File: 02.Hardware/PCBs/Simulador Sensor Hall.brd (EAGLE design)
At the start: 78.5 x 44.8 mm, 23 parts

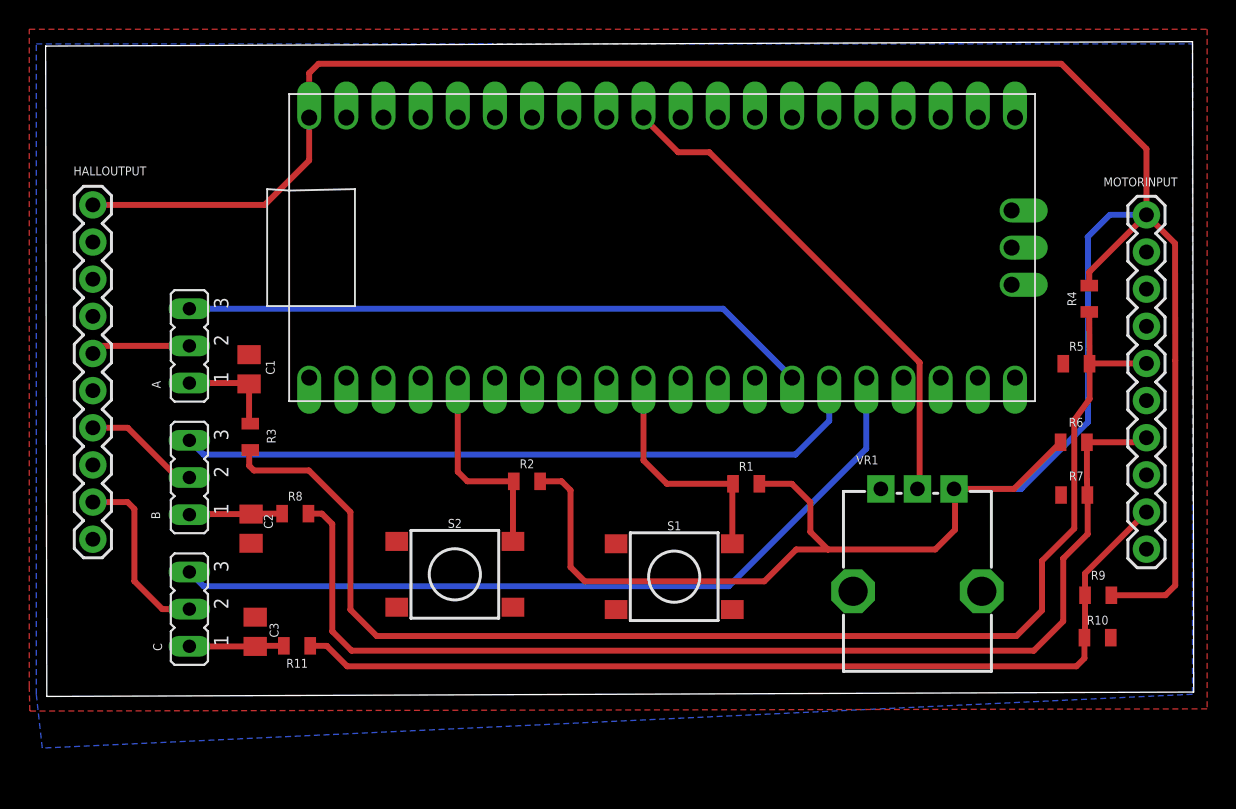
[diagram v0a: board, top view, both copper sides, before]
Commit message: Resistencias en serie en los pulsadores y potenciometro
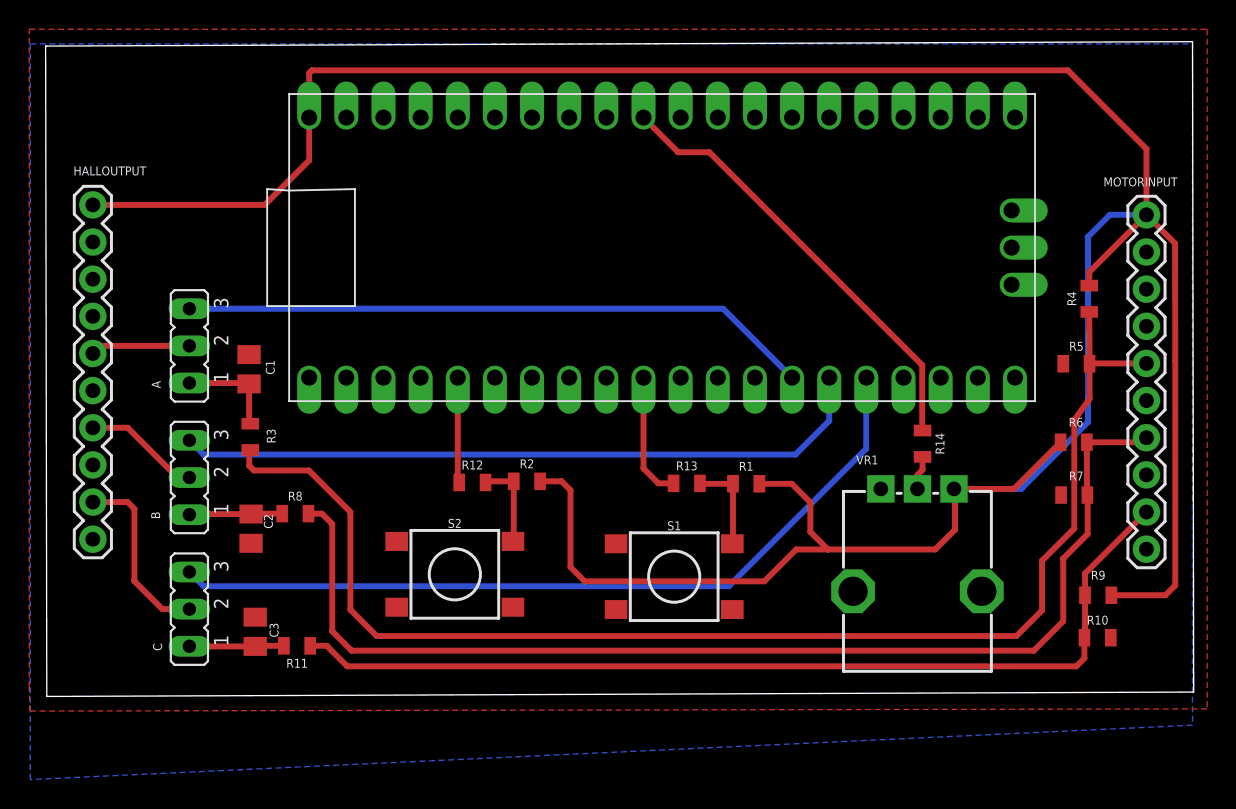
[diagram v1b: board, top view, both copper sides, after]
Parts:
- added R12, R13, R14: (no value), SparkFun-Resistors:0805
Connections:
- new net N$4: R12.2, R2.1, S2.B2
- new net N$6: R1.1, R13.2, S1.B2
- new net N$8: R14.2, VR1.P$2
- net DIR: now also R13.1; no longer R1.1, S1.B2
- net SPEED: now also R14.1; no longer VR1.P$2
- net START_STOP: now also R12.1; no longer R2.1, S2.B2
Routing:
- net DIR: track 16.6 -> 8.69 mm
- net START_STOP: track 14.7 -> 7.21 mm
- net N$6: track 0.00 -> 6.39 mm
- net N$4: track 0.00 -> 6.10 mm
- net SPEED: track 34.5 -> 30.6 mm
- net N$8: track 0.00 -> 2.33 mm
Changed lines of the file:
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@@
 <drawing>
 <settings>
-<setting alwaysvectorfont="yes"/>
+<setting alwaysvectorfont="no"/>
 <setting verticaltext="up"/>
 </settings>
@@
 <attribute name="VALUE" x="24.09" y="3.27" size="1.016" layer="27" rot="R90"/>
 </element>
+<element name="R12" library="SparkFun-Resistors" library_urn="urn:adsk.eagle:library:532" package="0805" package3d_urn="urn:adsk.eagle:package:39651/1" value=" " x="37.04" y="14.48" smashed="yes">
+<attribute name="NAME" x="37.04" y="15.369" size="0.6096" layer="25" font="vector" ratio="20" align="bottom-center"/>
+<attribute name="PROD_ID" value=" " x="37.29" y="14.48" size="1.778" layer="27" display="off"/>
+<attribute name="VALUE" x="37.04" y="13.591" size="0.6096" layer="27" font="vector" ratio="20" align="top-center"/>
+</element>
+<element name="R13" library="SparkFun-Resistors" library_urn="urn:adsk.eagle:library:532" package="0805" package3d_urn="urn:adsk.eagle:package:39651/1" value=" " x="51.7" y="14.42" smashed="yes">
+<attribute name="NAME" x="51.7" y="15.309" size="0.6096" layer="25" font="vector" ratio="20" align="bottom-center"/>
+<attribute name="PROD_ID" value=" " x="51.95" y="14.42" size="1.778" layer="27" display="off"/>
+<attribute name="VALUE" x="51.7" y="13.531" size="0.6096" layer="27" font="vector" ratio="20" align="top-center"/>
+</element>
+<element name="R14" library="SparkFun-Resistors" library_urn="urn:adsk.eagle:library:532" package="0805" package3d_urn="urn:adsk.eagle:package:39651/1" value=" " x="67.82" y="17.13" smashed="yes" rot="R270">
+<attribute name="NAME" x="68.709" y="17.13" size="0.6096" layer="25" font="vector" ratio="20" rot="R270" align="bottom-center"/>
+<attribute name="PROD_ID" value=" " x="67.82" y="16.88" size="1.778" layer="27" rot="R270" display="off"/>
+<attribute name="VALUE" x="66.931" y="17.13" size="0.6096" layer="27" font="vector" ratio="20" rot="R270" align="top-center"/>
+</element>
 </elements>
 <signals>
@@
 <wire x1="25.88" y1="36.5" x2="25.88" y2="39.43" width="0.4064" layer="1"/>
 <wire x1="25.88" y1="39.43" x2="25.88" y2="42.47" width="0.4064" layer="1"/>
-<wire x1="25.88" y1="42.47" x2="26.52" y2="43.11" width="0.4064" layer="1"/>
-<wire x1="26.52" y1="43.11" x2="77.31" y2="43.11" width="0.4064" layer="1"/>
+<wire x1="25.88" y1="42.47" x2="26.07" y2="42.66" width="0.4064" layer="1"/>
+<wire x1="26.07" y1="42.66" x2="77.76" y2="42.66" width="0.4064" layer="1"/>
 <wire x1="83.13" y1="37.29" x2="83.13" y2="32.78" width="0.4064" layer="1"/>
-<wire x1="77.31" y1="43.11" x2="83.13" y2="37.29" width="0.4064" layer="1"/>
+<wire x1="77.76" y1="42.66" x2="83.13" y2="37.29" width="0.4064" layer="1"/>
 <contactref element="R4" pad="2"/>
 <contactref element="R6" pad="2"/>
@@
 </polygon>
 <polygon width="0.1524" layer="16">
-<vertex x="7.22" y="44.47"/>
+<vertex x="6.81" y="44.47"/>
 <vertex x="86.28" y="44.47"/>
-<vertex x="86.28" y="0"/>
-<vertex x="7.63" y="-3.68"/>
-<vertex x="7.22" y="0"/>
+<vertex x="86.28" y="-2.11416875"/>
+<vertex x="6.81" y="-5.832534375"/>
 </polygon>
 <contactref element="R7" pad="1"/>
@@
 </signal>
 <signal name="START_STOP">
-<contactref element="R2" pad="1"/>
-<contactref element="S2" pad="B2"/>
 <contactref element="X1" pad="GP3"/>
-<wire x1="39.815" y1="10.45" x2="39.815" y2="14.505" width="0.4064" layer="1"/>
-<wire x1="39.815" y1="14.505" x2="39.87" y2="14.56" width="0.4064" layer="1"/>
-<wire x1="39.87" y1="14.56" x2="36.7" y2="14.56" width="0.4064" layer="1"/>
-<wire x1="36.04" y1="21.65" x2="36.04" y2="15.22" width="0.4064" layer="1"/>
-<wire x1="36.7" y1="14.56" x2="36.04" y2="15.22" width="0.4064" layer="1"/>
+<contactref element="R12" pad="1"/>
+<wire x1="36.14" y1="14.48" x2="36.04" y2="14.58" width="0.4064" layer="1"/>
+<wire x1="36.04" y1="14.58" x2="36.04" y2="21.65" width="0.4064" layer="1"/>
 </signal>
 <signal name="DIR">
-<contactref element="R1" pad="1"/>
-<contactref element="S1" pad="B2"/>
 <contactref element="X1" pad="GP7"/>
-<wire x1="54.815" y1="10.29" x2="54.815" y2="14.345" width="0.4064" layer="1"/>
-<wire x1="54.815" y1="14.345" x2="54.86" y2="14.39" width="0.4064" layer="1"/>
-<wire x1="54.86" y1="14.39" x2="50.34" y2="14.39" width="0.4064" layer="1"/>
-<wire x1="48.74" y1="21.65" x2="48.74" y2="15.99" width="0.4064" layer="1"/>
-<wire x1="50.34" y1="14.39" x2="48.74" y2="15.99" width="0.4064" layer="1"/>
+<wire x1="48.74" y1="15.44" x2="48.74" y2="21.65" width="0.4064" layer="1"/>
+<contactref element="R13" pad="1"/>
+<wire x1="50.8" y1="14.42" x2="49.76" y2="14.42" width="0.4064" layer="1"/>
+<wire x1="49.76" y1="14.42" x2="48.74" y2="15.44" width="0.4064" layer="1"/>
 </signal>
 <signal name="SPEED">
-<contactref element="VR1" pad="P$2"/>
 <contactref element="X1" pad="GP26_A0"/>
-<wire x1="67.62" y1="22.68" x2="67.62" y2="14.19" width="0.4064" layer="1"/>
-<wire x1="67.62" y1="14.19" x2="67.47" y2="14.04" width="0.4064" layer="1"/>
-<wire x1="67.62" y1="22.68" x2="53.24" y2="37.06" width="0.4064" layer="1"/>
+<wire x1="67.8" y1="22.5" x2="53.24" y2="37.06" width="0.4064" layer="1"/>
 <wire x1="53.24" y1="37.06" x2="51.11" y2="37.06" width="0.4064" layer="1"/>
 <wire x1="51.11" y1="37.06" x2="48.74" y2="39.43" width="0.4064" layer="1"/>
+<contactref element="R14" pad="1"/>
+<wire x1="67.82" y1="18.03" x2="67.8" y2="18.05" width="0.4064" layer="1"/>
+<wire x1="67.8" y1="22.5" x2="67.8" y2="18.05" width="0.4064" layer="1"/>
 </signal>
 <signal name="N$1">
@@
 <wire x1="78.93" y1="8.26" x2="83.13" y2="12.46" width="0.4064" layer="1"/>
 </signal>
+<signal name="N$4">
+<contactref element="S2" pad="B2"/>
+<contactref element="R12" pad="2"/>
+<contactref element="R2" pad="1"/>
+<wire x1="37.94" y1="14.48" x2="38.02" y2="14.56" width="0.4064" layer="1"/>
+<wire x1="38.02" y1="14.56" x2="39.87" y2="14.56" width="0.4064" layer="1"/>
+<wire x1="39.87" y1="14.56" x2="39.87" y2="10.505" width="0.4064" layer="1"/>
+<wire x1="39.87" y1="10.505" x2="39.815" y2="10.45" width="0.4064" layer="1"/>
+</signal>
+<signal name="N$6">
+<contactref element="R13" pad="2"/>
+<contactref element="R1" pad="1"/>
+<contactref element="S1" pad="B2"/>
+<wire x1="54.86" y1="14.39" x2="52.63" y2="14.39" width="0.4064" layer="1"/>
+<wire x1="52.63" y1="14.39" x2="52.6" y2="14.42" width="0.4064" layer="1"/>
+<wire x1="54.86" y1="14.39" x2="54.86" y2="10.335" width="0.4064" layer="1"/>
+<wire x1="54.86" y1="10.335" x2="54.815" y2="10.29" width="0.4064" layer="1"/>
+</signal>
+<signal name="N$8">
+<contactref element="VR1" pad="P$2"/>
+<contactref element="R14" pad="2"/>
+<wire x1="67.82" y1="16.23" x2="67.82" y2="15.34" width="0.4064" layer="1"/>
+<wire x1="67.82" y1="15.34" x2="67.47" y2="14.99" width="0.4064" layer="1"/>
+<wire x1="67.47" y1="14.99" x2="67.47" y2="14.04" width="0.4064" layer="1"/>
+</signal>
 </signals>

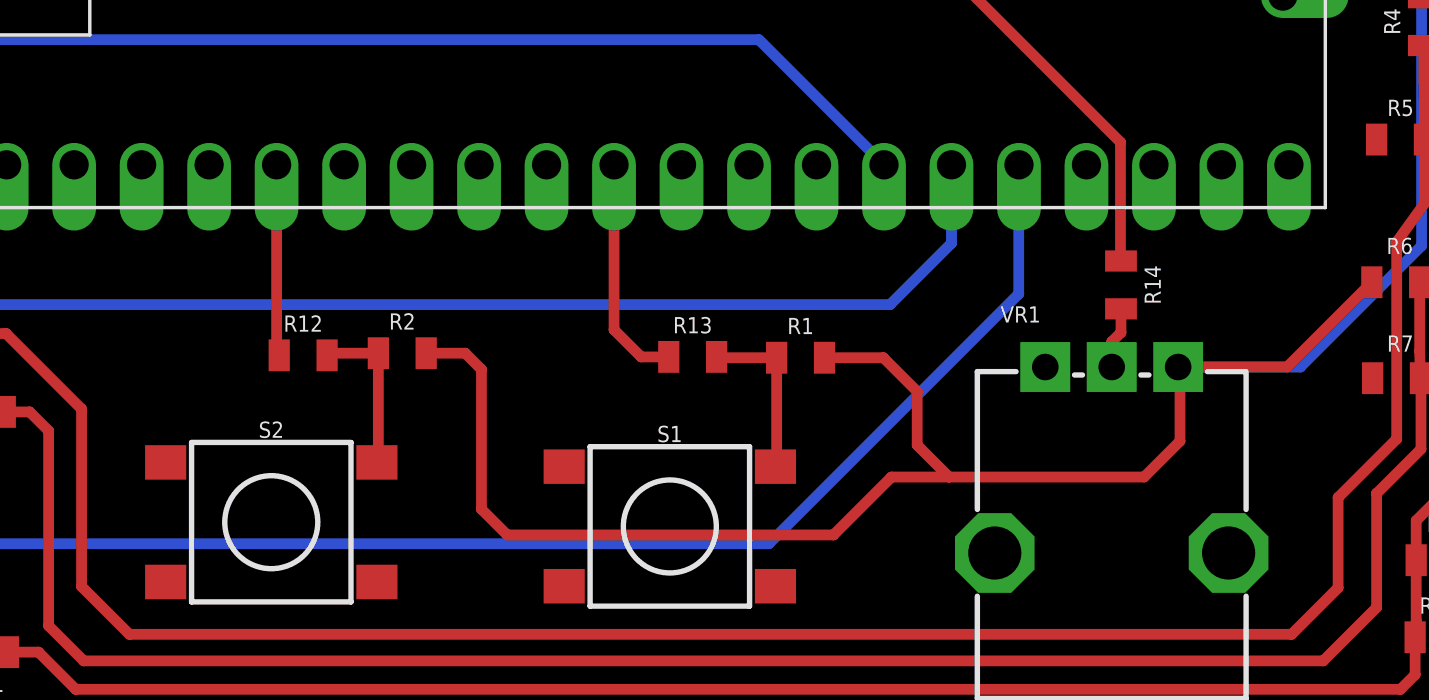
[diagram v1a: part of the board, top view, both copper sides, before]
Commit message: Add RC Antirebotes
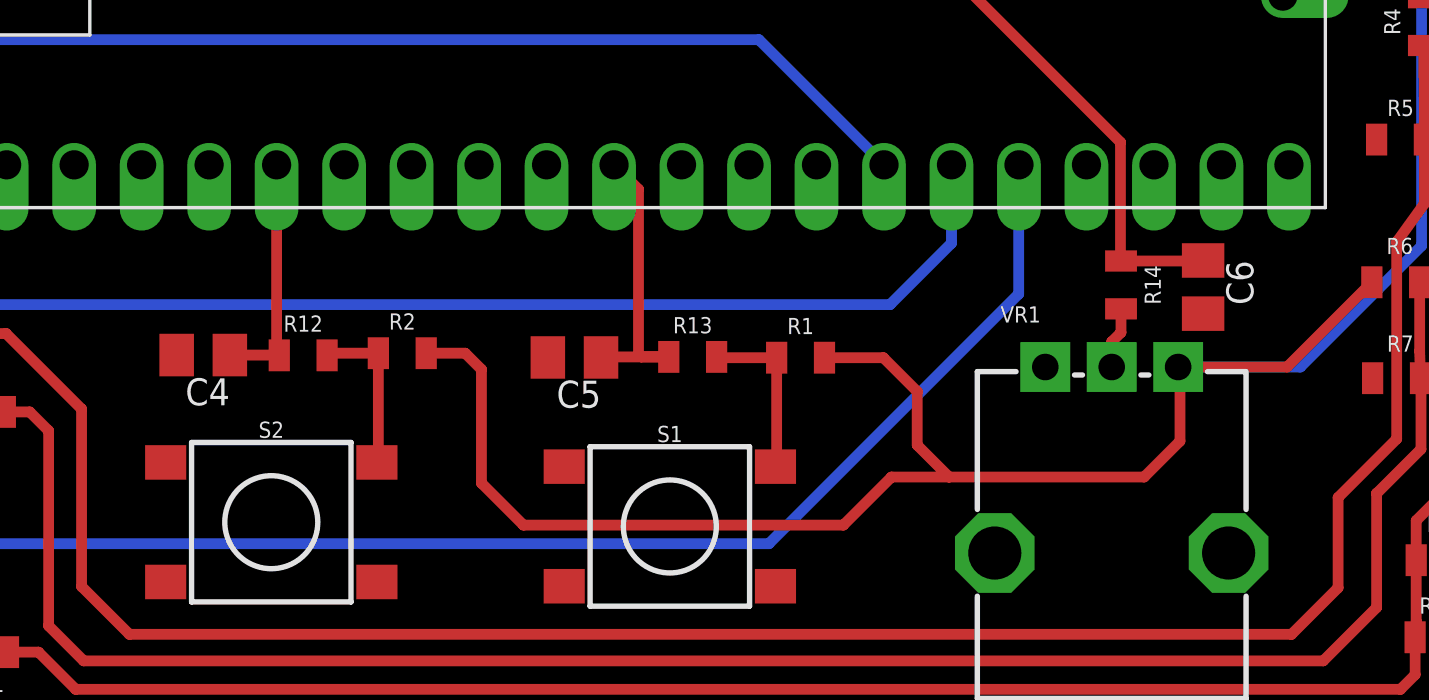
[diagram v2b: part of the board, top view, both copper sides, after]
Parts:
- added C4, C5, C6: (no value), rcl:C0805K
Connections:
- net DIR: now also C5.1
- net GND: now also C4.2, C5.2, C6.2
- net SPEED: now also C6.1
- net START_STOP: now also C4.1
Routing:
- net SPEED: track 30.6 -> 33.7 mm
- net DIR: track 8.69 -> 11.3 mm
- net START_STOP: track 7.21 -> 9.08 mm
- net VCC: track 206.6 -> 205.7 mm
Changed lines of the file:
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@@
 <attribute name="VALUE" x="66.931" y="17.13" size="0.6096" layer="27" font="vector" ratio="20" rot="R270" align="top-center"/>
+</element>
+<element name="C4" library="rcl" library_urn="urn:adsk.eagle:library:334" package="C0805K" package3d_urn="urn:adsk.eagle:package:23681/2" value="" x="33.28" y="14.49" smashed="yes" rot="R180">
+<attribute name="NAME" x="34.28" y="13.615" size="1.016" layer="25" rot="R180"/>
+<attribute name="POPULARITY" value="52" x="33.28" y="14.49" size="1.778" layer="27" rot="R180" display="off"/>
+<attribute name="SPICEPREFIX" value="C" x="33.28" y="14.49" size="1.778" layer="27" rot="R180" display="off"/>
+<attribute name="VALUE" x="34.28" y="16.39" size="1.016" layer="27" rot="R180"/>
+</element>
+<element name="C5" library="rcl" library_urn="urn:adsk.eagle:library:334" package="C0805K" package3d_urn="urn:adsk.eagle:package:23681/2" value="" x="47.25" y="14.4" smashed="yes" rot="R180">
+<attribute name="NAME" x="48.25" y="13.525" size="1.016" layer="25" rot="R180"/>
+<attribute name="POPULARITY" value="52" x="47.25" y="14.4" size="1.778" layer="27" rot="R180" display="off"/>
+<attribute name="SPICEPREFIX" value="C" x="47.25" y="14.4" size="1.778" layer="27" rot="R180" display="off"/>
+<attribute name="VALUE" x="48.25" y="16.3" size="1.016" layer="27" rot="R180"/>
+</element>
+<element name="C6" library="rcl" library_urn="urn:adsk.eagle:library:334" package="C0805K" package3d_urn="urn:adsk.eagle:package:23681/2" value="" x="70.91" y="17.05" smashed="yes" rot="R270">
+<attribute name="NAME" x="71.785" y="18.05" size="1.016" layer="25" rot="R270"/>
+<attribute name="POPULARITY" value="52" x="70.91" y="17.05" size="1.778" layer="27" rot="R270" display="off"/>
+<attribute name="SPICEPREFIX" value="C" x="70.91" y="17.05" size="1.778" layer="27" rot="R270" display="off"/>
+<attribute name="VALUE" x="69.01" y="18.05" size="1.016" layer="27" rot="R270"/>
 </element>
 </elements>
@@
 <wire x1="41.67" y1="14.56" x2="43.14" y2="14.56" width="0.4064" layer="1"/>
 <wire x1="43.14" y1="14.56" x2="43.75" y2="13.95" width="0.4064" layer="1"/>
-<wire x1="43.75" y1="13.95" x2="43.75" y2="8.69" width="0.4064" layer="1"/>
-<wire x1="43.75" y1="8.69" x2="44.72" y2="7.72" width="0.4064" layer="1"/>
-<wire x1="44.72" y1="7.72" x2="57" y2="7.72" width="0.4064" layer="1"/>
+<wire x1="43.75" y1="13.95" x2="43.75" y2="9.67" width="0.4064" layer="1"/>
+<wire x1="43.75" y1="9.67" x2="45.33" y2="8.09" width="0.4064" layer="1"/>
+<wire x1="45.33" y1="8.09" x2="57.37" y2="8.09" width="0.4064" layer="1"/>
 <wire x1="68.69" y1="9.9" x2="70.04" y2="11.25" width="0.4064" layer="1"/>
 <wire x1="70.04" y1="11.25" x2="70.04" y2="13.97" width="0.4064" layer="1"/>
 <wire x1="70.04" y1="13.97" x2="69.97" y2="14.04" width="0.4064" layer="1"/>
-<wire x1="57" y1="7.72" x2="59.18" y2="9.9" width="0.4064" layer="1"/>
+<wire x1="57.37" y1="8.09" x2="59.18" y2="9.9" width="0.4064" layer="1"/>
 <wire x1="59.18" y1="9.9" x2="61.35" y2="9.9" width="0.4064" layer="1"/>
 <wire x1="61.35" y1="9.9" x2="68.69" y2="9.9" width="0.4064" layer="1"/>
@@
 <contactref element="C2" pad="2"/>
 <contactref element="C3" pad="2"/>
+<contactref element="C4" pad="2"/>
+<contactref element="C5" pad="2"/>
+<contactref element="C6" pad="2"/>
 </signal>
 <signal name="HALL_A_IN">
@@
 <wire x1="36.14" y1="14.48" x2="36.04" y2="14.58" width="0.4064" layer="1"/>
 <wire x1="36.04" y1="14.58" x2="36.04" y2="21.65" width="0.4064" layer="1"/>
+<contactref element="C4" pad="1"/>
+<wire x1="34.28" y1="14.49" x2="36.13" y2="14.49" width="0.4064" layer="1"/>
+<wire x1="36.13" y1="14.49" x2="36.14" y2="14.48" width="0.4064" layer="1"/>
 </signal>
 <signal name="DIR">
 <contactref element="X1" pad="GP7"/>
-<wire x1="48.74" y1="15.44" x2="48.74" y2="21.65" width="0.4064" layer="1"/>
+<wire x1="49.66" y1="20.73" x2="49.66" y2="14.52" width="0.4064" layer="1"/>
+<wire x1="49.66" y1="20.73" x2="48.74" y2="21.65" width="0.4064" layer="1"/>
 <contactref element="R13" pad="1"/>
 <wire x1="50.8" y1="14.42" x2="49.76" y2="14.42" width="0.4064" layer="1"/>
-<wire x1="49.76" y1="14.42" x2="48.74" y2="15.44" width="0.4064" layer="1"/>
+<contactref element="C5" pad="1"/>
+<wire x1="50.8" y1="14.42" x2="48.27" y2="14.42" width="0.4064" layer="1"/>
+<wire x1="48.25" y1="14.4" x2="48.27" y2="14.42" width="0.4064" layer="1"/>
+<wire x1="49.66" y1="14.52" x2="49.76" y2="14.42" width="0.4064" layer="1"/>
 </signal>
 <signal name="SPEED">
@@
 <wire x1="67.82" y1="18.03" x2="67.8" y2="18.05" width="0.4064" layer="1"/>
 <wire x1="67.8" y1="22.5" x2="67.8" y2="18.05" width="0.4064" layer="1"/>
+<contactref element="C6" pad="1"/>
+<wire x1="70.91" y1="18.05" x2="70.91" y2="18.03" width="0.4064" layer="1"/>
+<wire x1="70.91" y1="18.03" x2="67.82" y2="18.03" width="0.4064" layer="1"/>
 </signal>
 <signal name="N$1">
